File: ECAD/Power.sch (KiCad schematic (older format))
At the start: 27 parts, among them J4 USB_C_Receptacle, Q1 SMD-MOSFET-P-CH-8V-4.1A-CJ230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, U1 AMS1117-3.3, U10 AP2127K-2.5, U4 ATtiny10-TS, U6 TPD2EUSB30, U7 AP2127K-2.8, U9 AP2127K-1.2

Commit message: V004 Update
Added ICSP pads
Updated 74LVC2G74 footprint
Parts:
- removed Q1: SMD-MOSFET-P-CH-8V-4.1A-CJ2305_SOT-23_, Package_TO_SOT_SMD:SOT-23, symbol OPL_Discrete_Semiconductor:SMD-MOSFET-P-CH-8V-4.1A-CJ2305_SOT-23_
- added Q1: SMD-MOSFET-N-CH-20V-2.1A-CJ2302_SOT-23_, Package_TO_SOT_SMD:SOT-23, symbol OPL_Discrete_Semiconductor:SMD-MOSFET-N-CH-20V-2.1A-CJ2302_SOT-23_
- added R15: 1.6K, Resistor_SMD:R_0402_1005Metric, symbol Device:R_Small
- added TP1, TP2, TP3, TP4, TP5: TestPoint, TestPoint:TestPoint_Pad_1.0x1.0mm, symbol Connector:TestPoint
- U4: value ATtiny10-TS -> ATTINY10-MAHR; footprint Package_TO_SOT_SMD:SOT-23-6_Handsoldering -> Package_DFN_QFN:DFN-8-1EP_2x2mm_P0.5mm_EP0.9x1.5mm; symbol MCU_Microchip_ATtiny:ATtiny10-TS -> MCU_Microchip_ATtiny:ATtiny10-MA; MPN ATtiny10-TS -> ATTINY10-MAHR
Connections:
- net +5V: now also U4.7 (VCC), TP1.1; no longer U4.5 (VCC)
- net 1V2_EN: now also U4.1 (PB1), TP3.1; no longer U4.3 (PB1)
- net 2V5_EN: now also U4.5 (PB0), TP4.1; no longer U4.4 (PB2)
- net 2V8_EN: now also U4.8 (PB2); no longer U4.1 (PB0)
- net AT_TINY_RST: now also TP2.1
- net FLASH_SIG: now also R15.1
- net GND: now also U4.4 (GND), TP5.1; no longer U4.2 (GND)
- net LED_V+: now also Q1.3 (D)
- net VIN: now also Q1.2 (S)
- new net: Q1.1 (G), R15.2
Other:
- note added: "TPI Pads"
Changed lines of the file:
@@
 $EndComp
 $Comp
-L MCU_Microchip_ATtiny:ATtiny10-TS U?
+L MCU_Microchip_ATtiny:ATtiny10-MA U?
 U 1 1 602BB0D5
 P 1900 3400
@@
 AR Path="/5FE173C9/602BB0D5" Ref="U4"  Part="1"
 F 0 "U4" H 1370 3446 50  0000 R CNN
-F 1 "ATtiny10-TS" H 1370 3355 50  0000 R CNN
-F 2 "Package_TO_SOT_SMD:SOT-23-6_Handsoldering" H 1900 3400 50  0001 C CIN
+F 1 "ATTINY10-MAHR" H 1370 3355 50  0000 R CNN
+F 2 "Package_DFN_QFN:DFN-8-1EP_2x2mm_P0.5mm_EP0.9x1.5mm" H 1900 3400 50  0001 C CIN
 F 3 "http://ww1.microchip.com/downloads/en/DeviceDoc/Atmel-8127-AVR-8-bit-Microcontroller-ATtiny4-ATtiny5-ATtiny9-ATtiny10_Datasheet.pdf" H 1900 3400 50  0001 C CNN
-F 4 "ATtiny10-TS" H 1900 3400 50  0001 C CNN "MPN"
+F 4 "ATTINY10-MAHR" H 1900 3400 50  0001 C CNN "MPN"
 	1    1900 3400
 	1    0    0    -1
@@
 Text Label 2600 3400 0    50   ~ 0
 AT_TINY_RST
-Text Label 2650 3300 0    50   ~ 0
+Text Label 2650 3100 0    50   ~ 0
 2V5_EN
 $Comp
@@
 Wire Wire Line
 	2150 6300 2250 6300
-$Comp
-L OPL_Discrete_Semiconductor:SMD-MOSFET-P-CH-8V-4.1A-CJ2305_SOT-23_ Q1
-U 1 1 5FE50876
-P 5650 3100
-F 0 "Q1" H 5764 3142 45  0000 L CNN
-F 1 "SMD-MOSFET-P-CH-8V-4.1A-CJ2305_SOT-23_" H 5764 3058 45  0000 L CNN
-F 2 "Package_TO_SOT_SMD:SOT-23" H 5650 3100 50  0001 C CNN
-F 3 "" H 5650 3100 50  0001 C CNN
-F 4 "CJ2305" H 5680 3250 20  0001 C CNN "MPN"
-F 5 "305030014" H 5680 3250 20  0001 C CNN "SKU"
-	1    5650 3100
-	1    0    0    -1
-$EndComp
 Wire Wire Line
 	5550 3500 5650 3500
@@
 Wire Wire Line
 	5650 3500 5650 3300
-Text GLabel 5050 3100 0    50   Input ~ 0
-FLASH_SIG
-Wire Wire Line
-	5050 3100 5450 3100
 $Comp
 L Device:C_Small C?
@@
 Text GLabel 10200 1500 2    50   Input ~ 0
 VAA
-Text Label 2650 3100 0    50   ~ 0
+Text Label 2650 3300 0    50   ~ 0
 2V8_EN
 $Comp
@@
 NoConn ~ 1950 6650
 NoConn ~ 1950 6750
+$Comp
+L OPL_Discrete_Semiconductor:SMD-MOSFET-N-CH-20V-2.1A-CJ2302_SOT-23_ Q1
+U 1 1 5FF7EB6F
+P 5650 3100
+F 0 "Q1" H 5765 3058 45  0000 L CNN
+F 1 "SMD-MOSFET-N-CH-20V-2.1A-CJ2302_SOT-23_" H 5765 3142 45  0000 L CNN
+F 2 "Package_TO_SOT_SMD:SOT-23" H 5650 3100 50  0001 C CNN
+F 3 "" H 5650 3100 50  0001 C CNN
+F 4 "CJ2302" H 5680 3250 20  0001 C CNN "MPN"
+F 5 "305030015" H 5680 3250 20  0001 C CNN "SKU"
+	1    5650 3100
+	-1   0    0    1
+$EndComp
+Text GLabel 6250 3100 2    50   Input ~ 0
+FLASH_SIG
+$Comp
+L Device:R_Small R?
+U 1 1 5FFAC8FD
+P 6050 3100
+AR Path="/5FFAC8FD" Ref="R?"  Part="1"
+AR Path="/5FE173C9/5FFAC8FD" Ref="R15"  Part="1"
+F 0 "R15" H 6109 3146 50  0000 L CNN
+F 1 "1.6K" H 6109 3055 50  0000 L CNN
+F 2 "Resistor_SMD:R_0402_1005Metric" H 6050 3100 50  0001 C CNN
+F 3 "~" H 6050 3100 50  0001 C CNN
+F 4 "RC0402FR-070RL" H 6050 3100 50  0001 C CNN "MPN"
+	1    6050 3100
+	0    1    1    0
+$EndComp
+Wire Wire Line
+	5950 3100 5850 3100
+Wire Wire Line
+	6150 3100 6250 3100
+Text Label 6450 4750 2    50   ~ 0
+1V2_EN
+Text Label 6450 4600 2    50   ~ 0
+AT_TINY_RST
+Text Label 6450 4900 2    50   ~ 0
+2V5_EN
+$Comp
+L power:+5V #PWR?
+U 1 1 6011348E
+P 6450 4450
+AR Path="/6011348E" Ref="#PWR?"  Part="1"
+AR Path="/5FE173C9/6011348E" Ref="#PWR05"  Part="1"
+F 0 "#PWR05" H 6450 4300 50  0001 C CNN
+F 1 "+5V" V 6465 4578 50  0000 L CNN
+F 2 "" H 6450 4450 50  0001 C CNN
+F 3 "" H 6450 4450 50  0001 C CNN
+	1    6450 4450
+	0    -1   -1   0
+$EndComp
+$Comp
+L power:GND #PWR?
+U 1 1 60116512
+P 6450 5050
+AR Path="/60116512" Ref="#PWR?"  Part="1"
+AR Path="/5FE173C9/60116512" Ref="#PWR06"  Part="1"
+F 0 "#PWR06" H 6450 4800 50  0001 C CNN
+F 1 "GND" H 6455 4877 50  0000 C CNN
+F 2 "" H 6450 5050 50  0001 C CNN
+F 3 "" H 6450 5050 50  0001 C CNN
+	1    6450 5050
+	1    0    0    -1
+$EndComp
+Wire Wire Line
+	6450 5050 6700 5050
+Wire Wire Line
+	6450 4900 6700 4900
+Wire Wire Line
+	6450 4750 6700 4750
+Wire Wire Line
+	6450 4600 6700 4600
+Wire Wire Line
+	6450 4450 6700 4450
+Text Notes 6550 4300 0    50   ~ 0
+TPI Pads
+$Comp
+L Connector:TestPoint TP1
+U 1 1 6013B1E6
+P 6700 4450
+F 0 "TP1" V 6654 4638 50  0000 L CNN
+F 1 "TestPoint" V 6745 4638 50  0000 L CNN
+F 2 "TestPoint:TestPoint_Pad_1.0x1.0mm" H 6900 4450 50  0001 C CNN
+F 3 "~" H 6900 4450 50  0001 C CNN
+	1    6700 4450
+	0    1    1    0
+$EndComp
+$Comp
+L Connector:TestPoint TP2
+U 1 1 6013C929
+P 6700 4600
+F 0 "TP2" V 6654 4788 50  0000 L CNN
+F 1 "TestPoint" V 6745 4788 50  0000 L CNN
+F 2 "TestPoint:TestPoint_Pad_1.0x1.0mm" H 6900 4600 50  0001 C CNN
+F 3 "~" H 6900 4600 50  0001 C CNN
+	1    6700 4600
+	0    1    1    0
+$EndComp
+$Comp
+L Connector:TestPoint TP3
+U 1 1 6013FC61
+P 6700 4750
+F 0 "TP3" V 6654 4938 50  0000 L CNN
+F 1 "TestPoint" V 6745 4938 50  0000 L CNN
+F 2 "TestPoint:TestPoint_Pad_1.0x1.0mm" H 6900 4750 50  0001 C CNN
+F 3 "~" H 6900 4750 50  0001 C CNN
+	1    6700 4750
+	0    1    1    0
+$EndComp
+$Comp
+L Connector:TestPoint TP4
+U 1 1 60143077
+P 6700 4900
+F 0 "TP4" V 6654 5088 50  0000 L CNN
+F 1 "TestPoint" V 6745 5088 50  0000 L CNN
+F 2 "TestPoint:TestPoint_Pad_1.0x1.0mm" H 6900 4900 50  0001 C CNN
+F 3 "~" H 6900 4900 50  0001 C CNN
+	1    6700 4900
+	0    1    1    0
+$EndComp
+$Comp
+L Connector:TestPoint TP5
+U 1 1 60146332
+P 6700 5050
+F 0 "TP5" V 6654 5238 50  0000 L CNN
+F 1 "TestPoint" V 6745 5238 50  0000 L CNN
+F 2 "TestPoint:TestPoint_Pad_1.0x1.0mm" H 6900 5050 50  0001 C CNN
+F 3 "~" H 6900 5050 50  0001 C CNN
+	1    6700 5050
+	0    1    1    0
+$EndComp
 $EndSCHEMATC

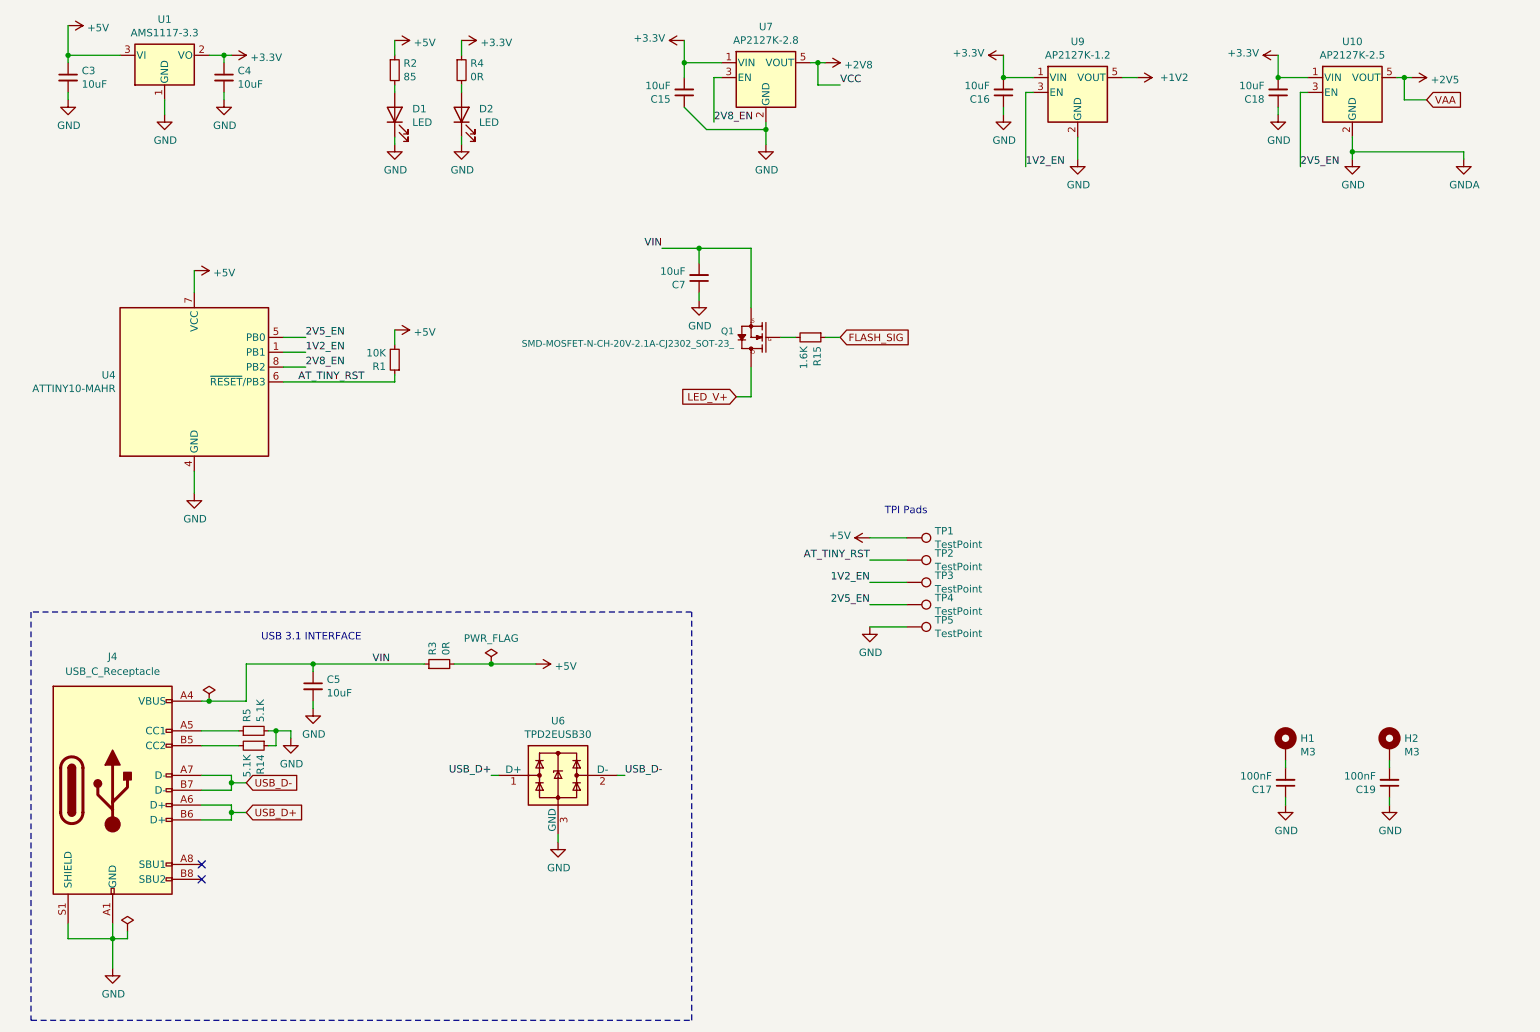
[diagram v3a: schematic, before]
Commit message: V005 Release
V0005 Replaces the ATTINY10 with an ATTINY1606, It also adds a breakaway expansion I/O and programming header.

The ATTINY is now on the I2C bus, and the flip/flop reset is now tied to the ATTINY GPIO.
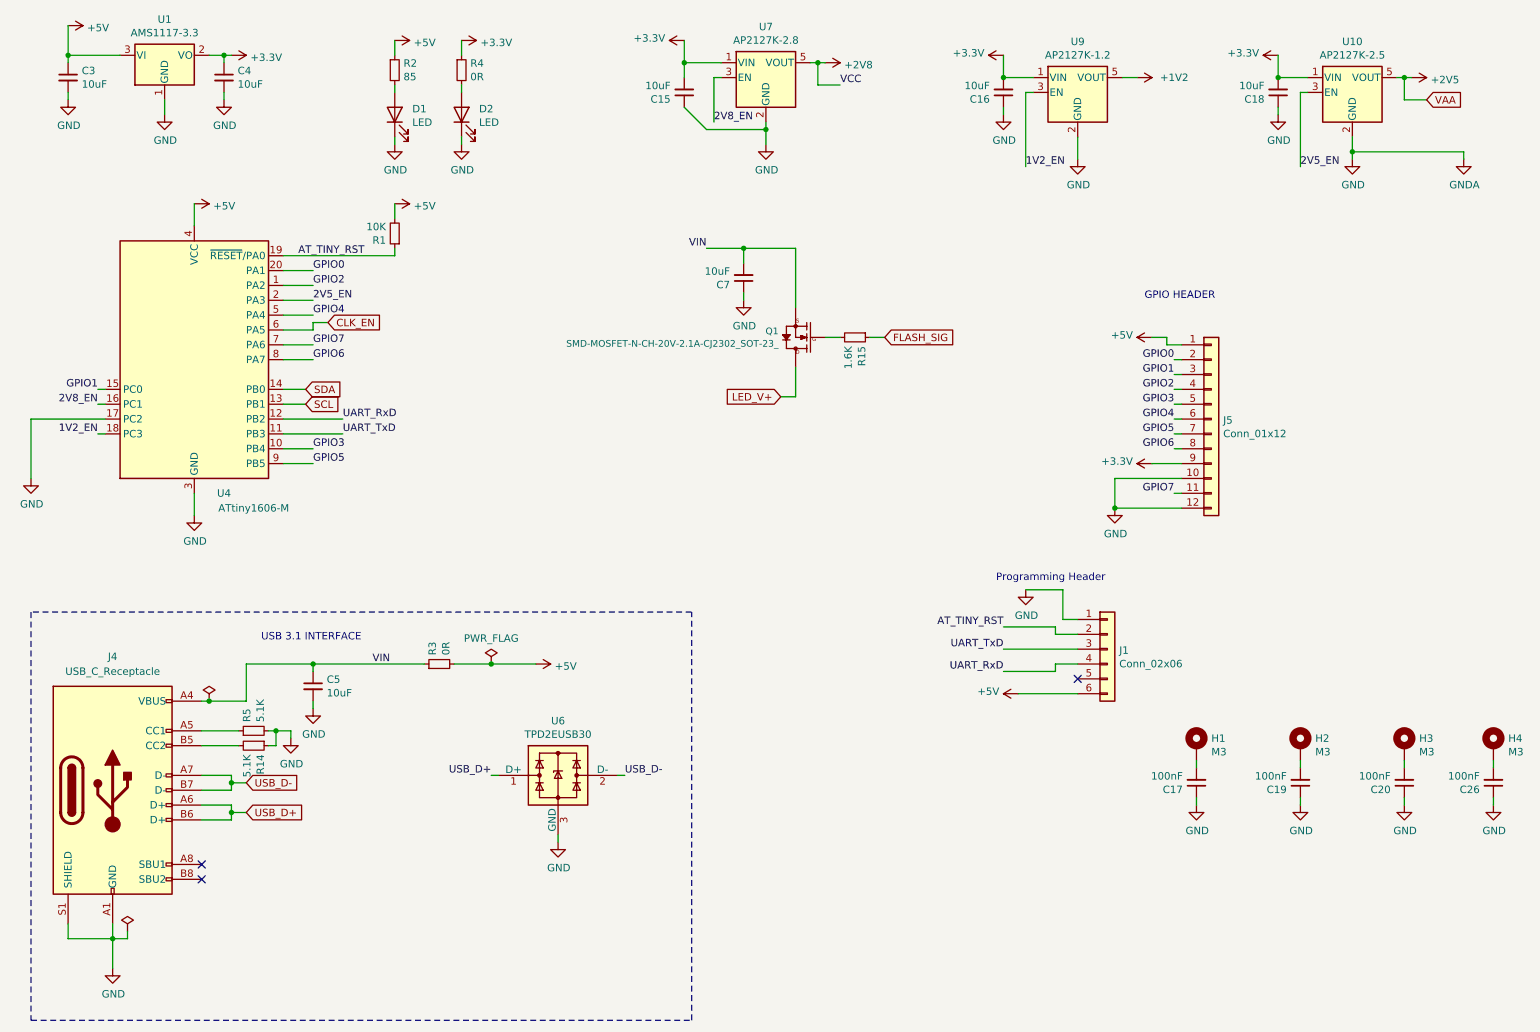
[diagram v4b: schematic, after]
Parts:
- removed TP1, TP2, TP3, TP4, TP5: TestPoint, TestPoint:TestPoint_Pad_1.0x1.0mm, symbol Connector:TestPoint
- removed U4: ATTINY10-MAHR, Package_DFN_QFN:DFN-8-1EP_2x2mm_P0.5mm_EP0.9x1.5mm, symbol MCU_Microchip_ATtiny:ATtiny10-MA
- added C20, C26: 100nF, Capacitor_SMD:C_0402_1005Metric, symbol Device:C_Small
- added H3, H4: M3, MountingHole:MountingHole_2.2mm_M2_Pad_Via, symbol Mechanical:MountingHole_Pad
- added J1: Conn_02x06, Connector_PinHeader_2.54mm:PinHeader_2x03_P2.54mm_Vertical, symbol Connector_Generic:Conn_01x06
- added J5: Conn_01x12, Connector_PinHeader_2.54mm:PinHeader_2x06_P2.54mm_Vertical, symbol Connector_Generic:Conn_01x12
- added U4: ATtiny1606-M, Package_DFN_QFN:VQFN-20-1EP_3x3mm_P0.4mm_EP1.7x1.7mm, symbol MCU_Microchip_ATtiny:ATtiny1606-M
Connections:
- net +3V3: now also J5.9 (Pin_9)
- net +5V: now also J1.6 (Pin_6), J5.1 (Pin_1), U4.4 (VCC)
- net 1V2_EN: now also U4.18 (PC3)
- net 2V5_EN: now also U4.2 (PA3)
- net 2V8_EN: now also U4.16 (PC1)
- net AT_TINY_RST: now also J1.2 (Pin_2), U4.19 (~RESET~/PA0)
- net GND: now also C20.1, C26.1, J1.1 (Pin_1), J5.10 (Pin_10), J5.12 (Pin_12), U4.17 (PC2), U4.21 (GND), U4.3 (GND)
- new net: C20.2, H3.1
- new net: C26.2, H4.1
- new net CLK_EN: U4.6 (PA5)
- new net GPIO0: J5.2 (Pin_2), U4.20 (PA1)
- new net GPIO1: J5.3 (Pin_3), U4.15 (PC0)
- new net GPIO2: J5.4 (Pin_4), U4.1 (PA2)
- new net GPIO3: J5.5 (Pin_5), U4.10 (PB4)
- new net GPIO4: J5.6 (Pin_6), U4.5 (PA4)
- new net GPIO5: J5.7 (Pin_7), U4.9 (PB5)
- new net GPIO6: J5.8 (Pin_8), U4.8 (PA7)
- new net GPIO7: J5.11 (Pin_11), U4.7 (PA6)
- new net SCL: U4.13 (PB1)
- new net SDA: U4.14 (PB0)
- new net UART_RxD: J1.4 (Pin_4), U4.12 (PB2)
- new net UART_TxD: J1.3 (Pin_3), U4.11 (PB3)
- no-connect marks 2 -> 3
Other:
- note added: "GPIO HEADER"
- note added: "Programming Header"
- note removed: "TPI Pads"
- moved on the sheet: C17, C19, C7, H1, H2, Q1, R15
